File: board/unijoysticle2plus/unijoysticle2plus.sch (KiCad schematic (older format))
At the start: 44 parts, among them J1 DB9_Female, J2 DB9_Female, J3 USB_B_Micro, Q1 S8050, Q2 S8050, SW1 RESET, SW2 JOY SWAP, U1 74HC05, U2 74HC05, U3 74HC05, U4 ESP32-WROOM-32D, U5 AMS1117-3.3, U6 CH340C

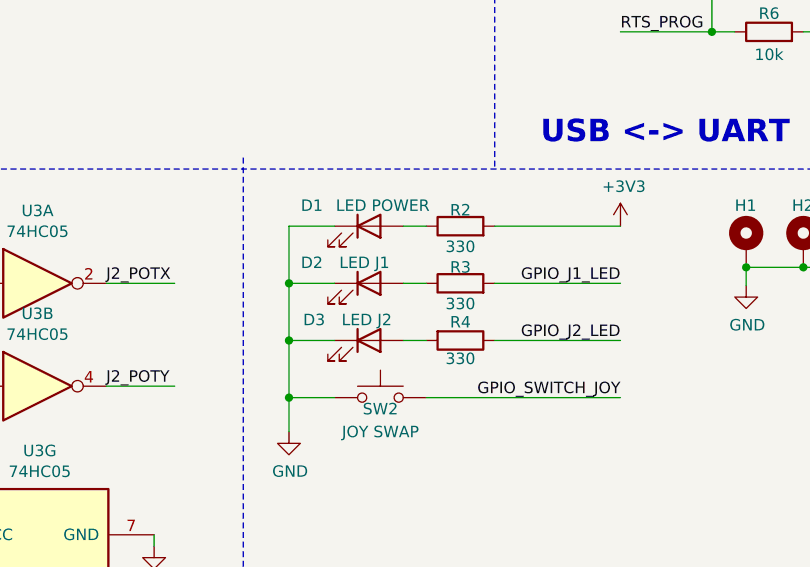
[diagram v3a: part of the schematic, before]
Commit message: unijoysticle2+: rev b. JLCPCB fixes
Add LCSC reference to new components
Update LCSC reference of old components to use 0805
Power plane in layer is split in 3: VCC (C64 5+), 3v3+ and VBUS
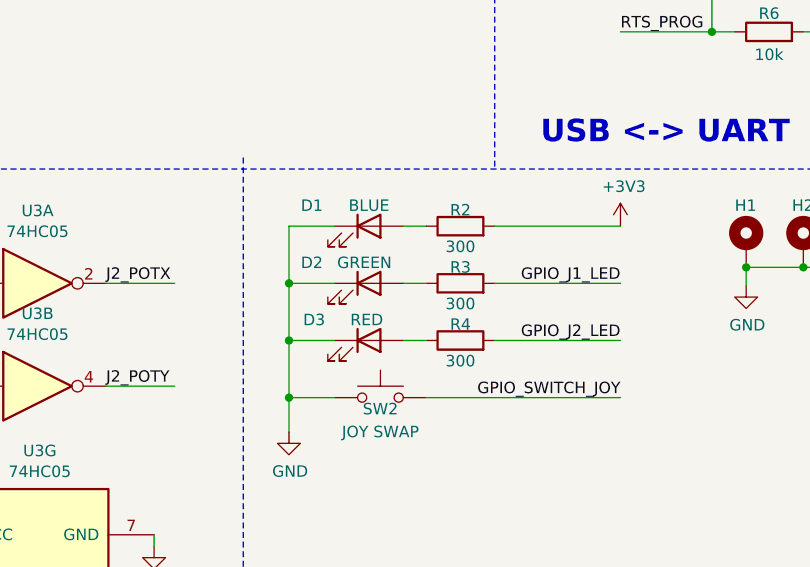
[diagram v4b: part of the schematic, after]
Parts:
- C1, C12, C2, C3, C4, C5: LCSC C1525 -> C49678
- C10: LCSC (none) -> C28323
- C11: LCSC (none) -> C49678
- C6, C8, C9: LCSC C59461 -> C45783
- D1: value LED POWER -> BLUE; LCSC (none) -> C389525
- D2: value LED J1 -> GREEN; LCSC (none) -> C188728
- D3: value LED J2 -> RED; LCSC (none) -> C84256
- R1, R5, R6: LCSC C25744 -> C17414
- R2, R3, R4: value 330 -> 300; LCSC (none) -> C17617
- R7, R8: LCSC (none) -> C17513
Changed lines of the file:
@@
 P 6150 6000
 F 0 "D2" H 5900 6090 50  0000 C CNN
-F 1 "LED J1" H 6130 6090 50  0000 C CNN
+F 1 "GREEN" H 6130 6090 50  0000 C CNN
 F 2 "LED_SMD:LED_0805_2012Metric_Pad1.15x1.40mm_HandSolder" H 6150 6000 50  0001 C CNN
 F 3 "~" H 6150 6000 50  0001 C CNN
-F 4 "" H 6150 6000 50  0001 C CNN "LCSC"
+F 4 "C188728" H 6150 6000 50  0001 C CNN "LCSC"
 	1    6150 6000
 	1    0    0    -1
@@
 P 6150 6250
 F 0 "D3" H 5910 6340 50  0000 C CNN
-F 1 "LED J2" H 6140 6340 50  0000 C CNN
+F 1 "RED" H 6140 6340 50  0000 C CNN
 F 2 "LED_SMD:LED_0805_2012Metric_Pad1.15x1.40mm_HandSolder" H 6150 6250 50  0001 C CNN
 F 3 "~" H 6150 6250 50  0001 C CNN
-F 4 "" H 6150 6250 50  0001 C CNN "LCSC"
+F 4 "C84256" H 6150 6250 50  0001 C CNN "LCSC"
 	1    6150 6250
 	1    0    0    -1
@@
 Wire Wire Line
 	6400 6500 7250 6500
-$Comp
-L Device:R R4
-U 1 1 5F9908EC
-P 6550 6250
-F 0 "R4" V 6470 6250 50  0000 C CNN
-F 1 "330" V 6630 6250 50  0000 C CNN
-F 2 "Resistor_SMD:R_0805_2012Metric_Pad1.20x1.40mm_HandSolder" V 6480 6250 50  0001 C CNN
-F 3 "~" H 6550 6250 50  0001 C CNN
-F 4 "" V 6550 6250 50  0001 C CNN "LCSC"
-	1    6550 6250
-	0    1    1    0
-$EndComp
 Wire Wire Line
 	6700 6000 7250 6000
@@
 F 2 "Capacitor_SMD:C_0805_2012Metric_Pad1.18x1.45mm_HandSolder" H 8300 1200 50  0001 C CNN
 F 3 "~" H 8300 1200 50  0001 C CNN
-F 4 "C59461" H 8300 1200 50  0001 C CNN "LCSC"
+F 4 "C45783" H 8300 1200 50  0001 C CNN "LCSC"
 	1    8300 1200
 	1    0    0    -1
@@
 F 2 "Capacitor_SMD:C_0805_2012Metric_Pad1.18x1.45mm_HandSolder" H 9200 1200 50  0001 C CNN
 F 3 "~" H 9200 1200 50  0001 C CNN
-F 4 "C59461" H 9200 1200 50  0001 C CNN "LCSC"
+F 4 "C45783" H 9200 1200 50  0001 C CNN "LCSC"
 	1    9200 1200
 	1    0    0    -1
@@
 F 2 "Resistor_SMD:R_0805_2012Metric_Pad1.20x1.40mm_HandSolder" V 7830 4350 50  0001 C CNN
 F 3 "~" H 7900 4350 50  0001 C CNN
-F 4 "C25744" V 7900 4350 50  0001 C CNN "LCSC"
+F 4 "C17414" V 7900 4350 50  0001 C CNN "LCSC"
 	1    7900 4350
 	0    1    1    0
@@
 F 2 "Resistor_SMD:R_0805_2012Metric_Pad1.20x1.40mm_HandSolder" V 7830 4900 50  0001 C CNN
 F 3 "~" H 7900 4900 50  0001 C CNN
-F 4 "C25744" V 7900 4900 50  0001 C CNN "LCSC"
+F 4 "C17414" V 7900 4900 50  0001 C CNN "LCSC"
 	1    7900 4900
 	0    -1   -1   0
@@
 F 2 "Capacitor_SMD:C_0805_2012Metric_Pad1.18x1.45mm_HandSolder" H 6000 1050 50  0001 C CNN
 F 3 "~" H 6000 1050 50  0001 C CNN
-F 4 "C59461" H 6000 1050 50  0001 C CNN "LCSC"
+F 4 "C45783" H 6000 1050 50  0001 C CNN "LCSC"
 	1    6000 1050
 	-1   0    0    1
@@
 F 2 "Capacitor_SMD:C_0805_2012Metric_Pad1.18x1.45mm_HandSolder" H 5600 1050 50  0001 C CNN
 F 3 "~" H 5600 1050 50  0001 C CNN
-F 4 "C1525" H 5600 1050 50  0001 C CNN "LCSC"
+F 4 "C49678" H 5600 1050 50  0001 C CNN "LCSC"
 	1    5600 1050
 	1    0    0    -1
@@
 F 2 "Capacitor_SMD:C_0805_2012Metric_Pad1.18x1.45mm_HandSolder" H 4210 7200 50  0001 C CNN
 F 3 "~" H 4210 7200 50  0001 C CNN
-F 4 "C1525" H 4210 7200 50  0001 C CNN "LCSC"
+F 4 "C49678" H 4210 7200 50  0001 C CNN "LCSC"
 	1    4210 7200
 	1    0    0    -1
@@
 F 2 "Capacitor_SMD:C_0805_2012Metric_Pad1.18x1.45mm_HandSolder" H 2560 7150 50  0001 C CNN
 F 3 "~" H 2560 7150 50  0001 C CNN
-F 4 "C1525" H 2560 7150 50  0001 C CNN "LCSC"
+F 4 "C49678" H 2560 7150 50  0001 C CNN "LCSC"
 	1    2560 7150
 	1    0    0    -1
@@
 F 2 "Capacitor_SMD:C_0805_2012Metric_Pad1.18x1.45mm_HandSolder" H 760 7150 50  0001 C CNN
 F 3 "~" H 760 7150 50  0001 C CNN
-F 4 "C1525" H 760 7150 50  0001 C CNN "LCSC"
+F 4 "C49678" H 760 7150 50  0001 C CNN "LCSC"
 	1    760  7150
 	1    0    0    -1
@@
 P 6150 5750
 F 0 "D1" H 5900 5840 50  0000 C CNN
-F 1 "LED POWER" H 6210 5840 50  0000 C CNN
+F 1 "BLUE" H 6150 5840 50  0000 C CNN
 F 2 "LED_SMD:LED_0805_2012Metric_Pad1.15x1.40mm_HandSolder" H 6150 5750 50  0001 C CNN
 F 3 "~" H 6150 5750 50  0001 C CNN
-F 4 "" H 6150 5750 50  0001 C CNN "LCSC"
+F 4 "C389525" H 6150 5750 50  0001 C CNN "LCSC"
 	1    6150 5750
 	1    0    0    -1
@@
 P 6550 5750
 F 0 "R2" V 6620 5750 50  0000 C CNN
-F 1 "330" V 6460 5750 50  0000 C CNN
+F 1 "300" V 6460 5750 50  0000 C CNN
 F 2 "Resistor_SMD:R_0805_2012Metric_Pad1.20x1.40mm_HandSolder" V 6480 5750 50  0001 C CNN
 F 3 "~" H 6550 5750 50  0001 C CNN
-F 4 "" V 6550 5750 50  0001 C CNN "LCSC"
+F 4 "C17617" V 6550 5750 50  0001 C CNN "LCSC"
 	1    6550 5750
 	0    -1   -1   0
@@
 P 6550 6000
 F 0 "R3" V 6620 6000 50  0000 C CNN
-F 1 "330" V 6460 6000 50  0000 C CNN
+F 1 "300" V 6460 6000 50  0000 C CNN
 F 2 "Resistor_SMD:R_0805_2012Metric_Pad1.20x1.40mm_HandSolder" V 6480 6000 50  0001 C CNN
 F 3 "~" H 6550 6000 50  0001 C CNN
-F 4 "" V 6550 6000 50  0001 C CNN "LCSC"
+F 4 "C17617" V 6550 6000 50  0001 C CNN "LCSC"
 	1    6550 6000
 	0    -1   -1   0
@@
 F 2 "Capacitor_SMD:C_0805_2012Metric_Pad1.18x1.45mm_HandSolder" H 3550 2480 50  0001 C CNN
 F 3 "~" H 3550 2480 50  0001 C CNN
-F 4 "C1525" V 3550 2480 50  0001 C CNN "LCSC"
+F 4 "C49678" V 3550 2480 50  0001 C CNN "LCSC"
 	1    3550 2480
 	0    -1   -1   0
@@
 F 2 "Resistor_SMD:R_0805_2012Metric_Pad1.20x1.40mm_HandSolder" V 4030 1270 50  0001 C CNN
 F 3 "~" H 4100 1270 50  0001 C CNN
-F 4 "C25744" V 4100 1270 50  0001 C CNN "LCSC"
+F 4 "C17414" V 4100 1270 50  0001 C CNN "LCSC"
 	1    4100 1270
 	-1   0    0    1
@@
 F 2 "Capacitor_SMD:C_0805_2012Metric_Pad1.18x1.45mm_HandSolder" H 4100 1700 50  0001 C CNN
 F 3 "~" H 4100 1700 50  0001 C CNN
-F 4 "C1525" H 4100 1700 50  0001 C CNN "LCSC"
+F 4 "C49678" H 4100 1700 50  0001 C CNN "LCSC"
 	1    4100 1700
 	1    0    0    -1
@@
 F 2 "Capacitor_SMD:C_0805_2012Metric_Pad1.18x1.45mm_HandSolder" H 9150 3050 50  0001 C CNN
 F 3 "~" H 9150 3050 50  0001 C CNN
+F 4 "C28323" H 9150 3050 50  0001 C CNN "LCSC"
 	1    9150 3050
 	1    0    0    -1
@@
 F 2 "Capacitor_SMD:C_0805_2012Metric_Pad1.18x1.45mm_HandSolder" H 10480 1920 50  0001 C CNN
 F 3 "~" H 10480 1920 50  0001 C CNN
+F 4 "C49678" H 10480 1920 50  0001 C CNN "LCSC"
 	1    10480 1920
 	1    0    0    -1
@@
 F 2 "Resistor_SMD:R_0805_2012Metric_Pad1.20x1.40mm_HandSolder" H 10180 2340 50  0001 C CNN
 F 3 "~" H 10180 2340 50  0001 C CNN
+F 4 "C17513" V 10180 2340 50  0001 C CNN "LCSC"
 	1    10180 2340
 	0    1    1    0
@@
 F 2 "Resistor_SMD:R_0805_2012Metric_Pad1.20x1.40mm_HandSolder" H 10180 2440 50  0001 C CNN
 F 3 "~" H 10180 2440 50  0001 C CNN
+F 4 "C17513" V 10180 2440 50  0001 C CNN "LCSC"
 	1    10180 2440
 	0    1    1    0
@@
 Wire Wire Line
 	10280 2440 10620 2440
+$Comp
+L Device:R R4
+U 1 1 61258BA1
+P 6550 6250
+F 0 "R4" V 6620 6250 50  0000 C CNN
+F 1 "300" V 6460 6250 50  0000 C CNN
+F 2 "Resistor_SMD:R_0805_2012Metric_Pad1.20x1.40mm_HandSolder" V 6480 6250 50  0001 C CNN
+F 3 "~" H 6550 6250 50  0001 C CNN
+F 4 "C17617" V 6550 6250 50  0001 C CNN "LCSC"
+	1    6550 6250
+	0    -1   -1   0
+$EndComp
 $EndSCHEMATC

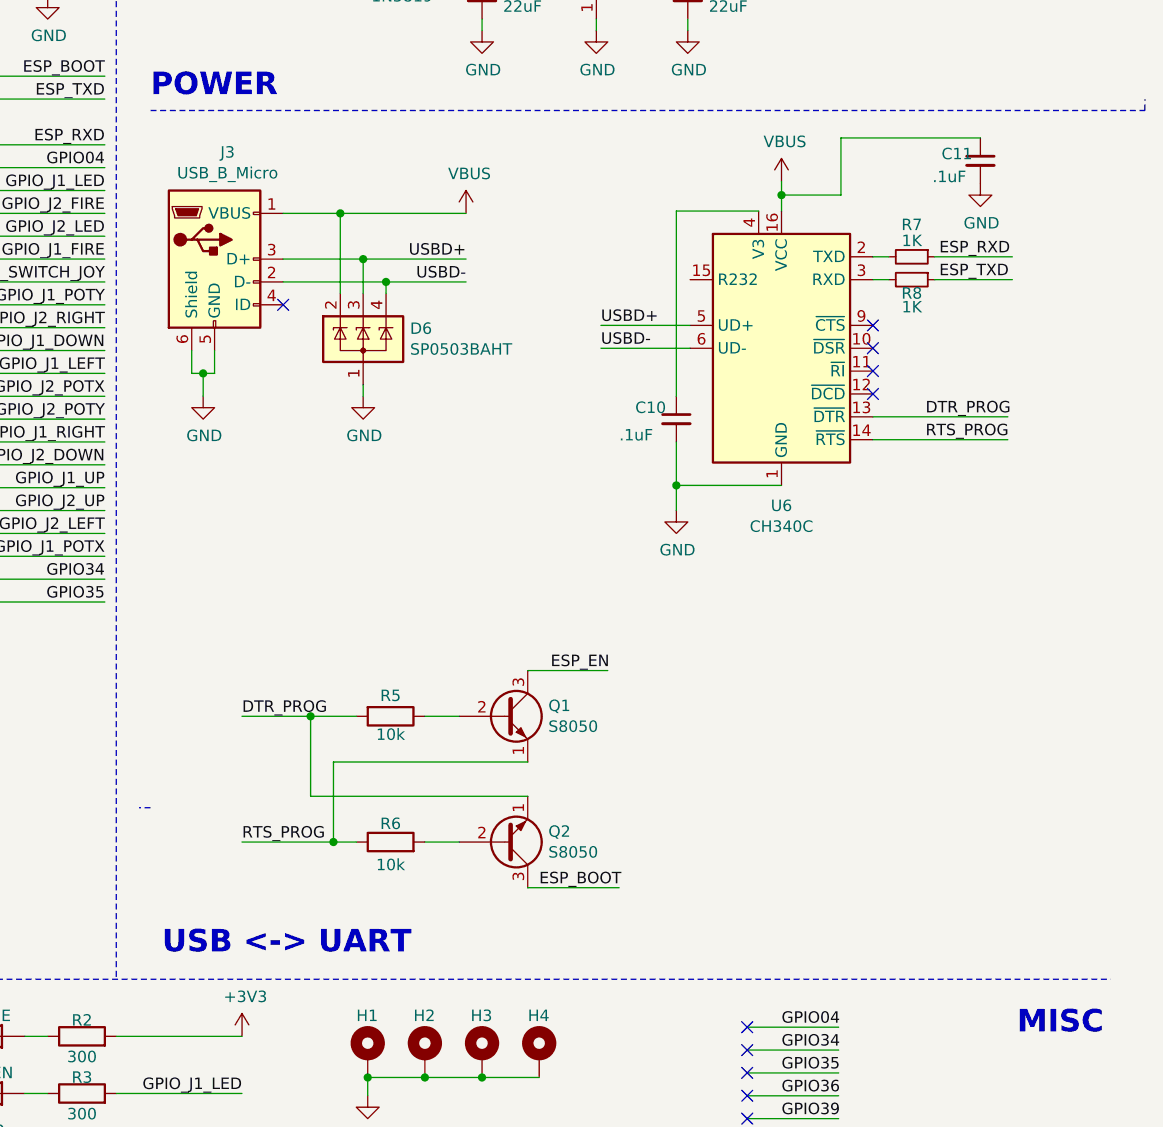
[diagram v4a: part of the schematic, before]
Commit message: Unijoysticle2+: Rev C. WIP
Although I haven't tested yet Rev B., there a few changes that I wanted
to make to it.
Rev. C, so far, has the following changes:

- Switch Power plane with Ground place: Ground plane is #2 and Power
  plane #3.
- Manually routed: No longer uses auto-route. I think it is better for
  debugging to route it manually. More vias. Vias placed closer to the
  pads. Might reduce inductance (?).
- No longer using the ESD protector for USB. Almost nobody uses it,
  besides that CP2104 recommends it. But I'm no longer using CP2104, and
  CH340 doesn't mention it... I think it would be a good idea
  nonetheless, but only as an optional feature.
- Differential pair routing for USB D- and USB D+
- Mounting holes moved a tiny bit closer to the corners

Again, Rev. B might work perfectly well... waiting for it to arrive. But
I just wanted to make the above mentioned changes.
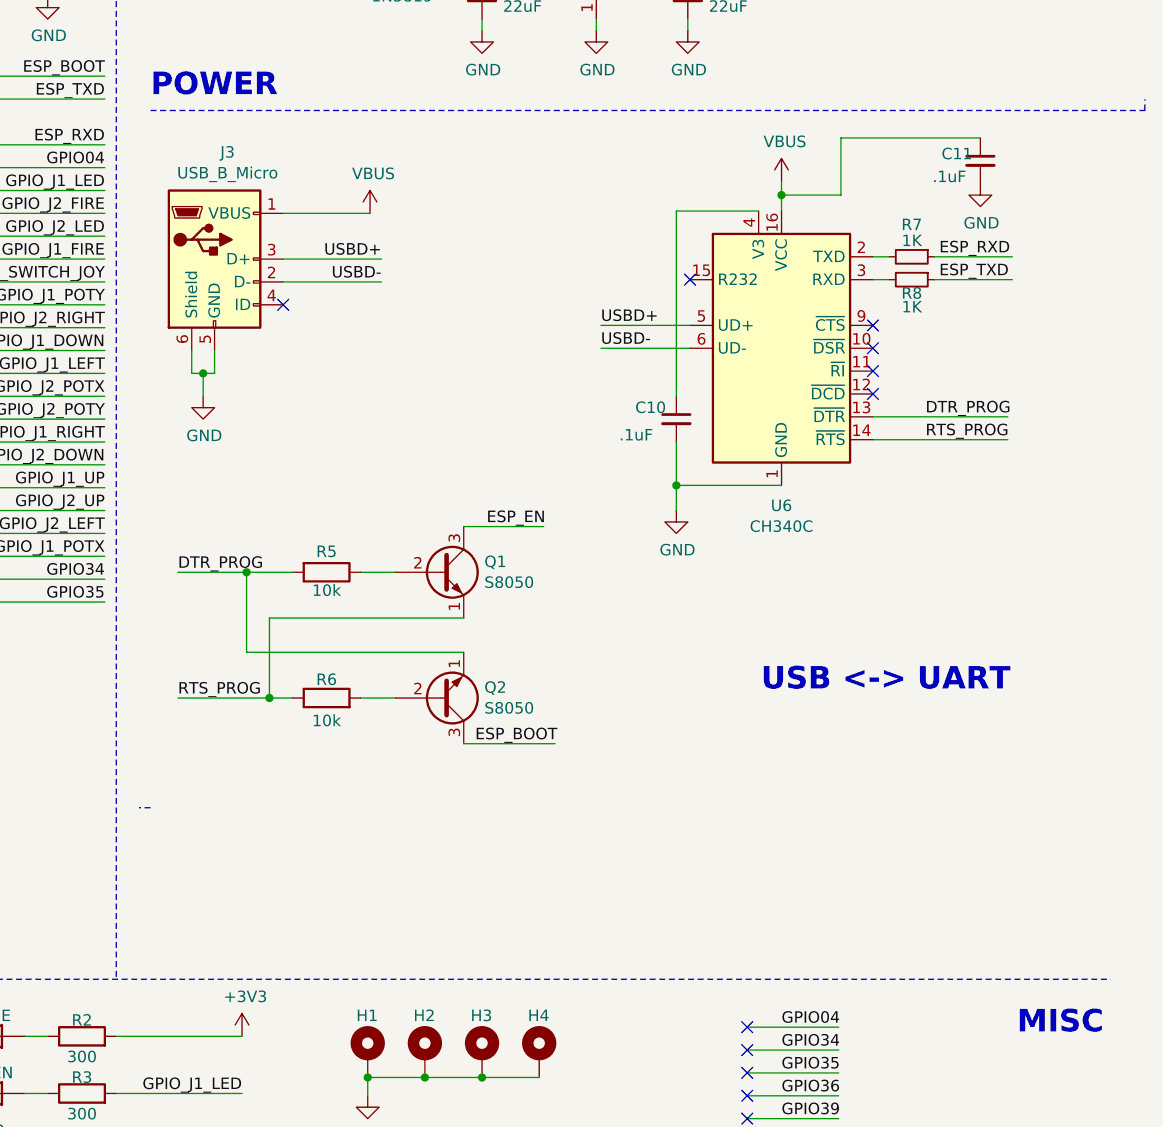
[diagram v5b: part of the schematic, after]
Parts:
- removed D6: SP0503BAHT, Package_TO_SOT_SMD:SOT-143, symbol Power_Protection:SP0503BAHT
- R9: footprint Resistor_SMD:R_1206_3216Metric_Pad1.30x1.75mm_HandSolder -> Resistor_SMD:R_0805_2012Metric_Pad1.20x1.40mm_HandSolder; LCSC C17888 -> C17477
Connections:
- wire segments 196 -> 189
- no-connect marks 17 -> 18
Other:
- moved on the sheet: Q1, Q2, R5, R6
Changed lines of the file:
@@
 Sheet 1 1
 Title "Unijoysticle 2+"
-Date "2021-06-22"
-Rev "B"
+Date "2021-06-25"
+Rev "C"
 Comp "Retro Moe"
 Comment1 ""
@@
 	1    0    0    -1
 $EndComp
-Wire Wire Line
-	7680 2500 7680 2150
-Wire Wire Line
-	7680 2150 7430 2150
-$Comp
-L power:GND #PWR023
-U 1 1 5FCD484D
-P 7780 2950
-F 0 "#PWR023" H 7780 2700 50  0001 C CNN
-F 1 "GND" H 7785 2777 50  0000 C CNN
-F 2 "" H 7780 2950 50  0001 C CNN
-F 3 "" H 7780 2950 50  0001 C CNN
-	1    7780 2950
-	1    0    0    -1
-$EndComp
-Text Label 8230 2350 2    50   ~ 0
+Text Label 7860 2350 2    50   ~ 0
 USBD+
-Text Label 8230 2450 2    50   ~ 0
+Text Label 7860 2450 2    50   ~ 0
 USBD-
-Connection ~ 7680 2150
 $Comp
 L Diode:1N5819 D4
@@
 	-1   0    0    1
 $EndComp
-Wire Wire Line
-	7680 2150 8230 2150
 $Comp
 L power:VBUS #PWR025
 U 1 1 5FD77036
-P 8230 2150
-F 0 "#PWR025" H 8230 2000 50  0001 C CNN
-F 1 "VBUS" H 8245 2323 50  0000 C CNN
-F 2 "" H 8230 2150 50  0001 C CNN
-F 3 "" H 8230 2150 50  0001 C CNN
-	1    8230 2150
+P 7810 2150
+F 0 "#PWR025" H 7810 2000 50  0001 C CNN
+F 1 "VBUS" H 7825 2323 50  0000 C CNN
+F 2 "" H 7810 2150 50  0001 C CNN
+F 3 "" H 7810 2150 50  0001 C CNN
+	1    7810 2150
 	1    0    0    -1
 $EndComp
@@
 $EndComp
 Wire Wire Line
-	8500 5100 8900 5100
-Wire Wire Line
-	8200 4350 8050 4350
-Wire Wire Line
-	8200 4900 8050 4900
+	8220 4470 8620 4470
+Wire Wire Line
+	7920 3720 7770 3720
+Wire Wire Line
+	7920 4270 7770 4270
 $Comp
 L Device:R R5
 U 1 1 60AF2CFC
-P 7900 4350
-F 0 "R5" V 7810 4350 50  0000 C CNN
-F 1 "10k" V 7980 4350 50  0000 C CNN
-F 2 "Resistor_SMD:R_0805_2012Metric_Pad1.20x1.40mm_HandSolder" V 7830 4350 50  0001 C CNN
-F 3 "~" H 7900 4350 50  0001 C CNN
-F 4 "C17414" V 7900 4350 50  0001 C CNN "LCSC"
-	1    7900 4350
+P 7620 3720
+F 0 "R5" V 7530 3720 50  0000 C CNN
+F 1 "10k" V 7700 3720 50  0000 C CNN
+F 2 "Resistor_SMD:R_0805_2012Metric_Pad1.20x1.40mm_HandSolder" V 7550 3720 50  0001 C CNN
+F 3 "~" H 7620 3720 50  0001 C CNN
+F 4 "C17414" V 7620 3720 50  0001 C CNN "LCSC"
+	1    7620 3720
 	0    1    1    0
 $EndComp
@@
 L Device:R R6
 U 1 1 60AF3FED
-P 7900 4900
-F 0 "R6" V 7980 4900 50  0000 C CNN
-F 1 "10k" V 7800 4900 50  0000 C CNN
-F 2 "Resistor_SMD:R_0805_2012Metric_Pad1.20x1.40mm_HandSolder" V 7830 4900 50  0001 C CNN
-F 3 "~" H 7900 4900 50  0001 C CNN
-F 4 "C17414" V 7900 4900 50  0001 C CNN "LCSC"
-	1    7900 4900
+P 7620 4270
+F 0 "R6" V 7700 4270 50  0000 C CNN
+F 1 "10k" V 7520 4270 50  0000 C CNN
+F 2 "Resistor_SMD:R_0805_2012Metric_Pad1.20x1.40mm_HandSolder" V 7550 4270 50  0001 C CNN
+F 3 "~" H 7620 4270 50  0001 C CNN
+F 4 "C17414" V 7620 4270 50  0001 C CNN "LCSC"
+	1    7620 4270
 	0    -1   -1   0
 $EndComp
 Wire Wire Line
-	7750 4350 7550 4350
-Wire Wire Line
-	7750 4900 7650 4900
-Wire Wire Line
-	8500 4550 7650 4550
-Wire Wire Line
-	7650 4550 7650 4900
-Connection ~ 7650 4900
-Wire Wire Line
-	7550 4350 7550 4700
-Wire Wire Line
-	7550 4350 7250 4350
-Connection ~ 7550 4350
-Wire Wire Line
-	7250 4900 7650 4900
-Wire Wire Line
-	8500 4150 8850 4150
+	7470 3720 7270 3720
+Wire Wire Line
+	7470 4270 7370 4270
+Wire Wire Line
+	8220 3920 7370 3920
+Wire Wire Line
+	7370 3920 7370 4270
+Connection ~ 7370 4270
+Wire Wire Line
+	7270 3720 7270 4070
+Wire Wire Line
+	7270 3720 6970 3720
+Connection ~ 7270 3720
+Wire Wire Line
+	6970 4270 7370 4270
+Wire Wire Line
+	8220 3520 8570 3520
 $Comp
 L Connector:USB_B_Micro J3
@@
 	1    0    0    -1
 $EndComp
-Text Label 7250 4350 0    50   ~ 0
+Text Label 6970 3720 0    50   ~ 0
 DTR_PROG
-Text Label 7250 4900 0    50   ~ 0
+Text Label 6970 4270 0    50   ~ 0
 RTS_PROG
-Text Label 8550 5100 0    50   ~ 0
+Text Label 8270 4470 0    50   ~ 0
 ESP_BOOT
-Text Label 8600 4150 0    50   ~ 0
+Text Label 8320 3520 0    50   ~ 0
 ESP_EN
 Wire Wire Line
@@
 L Transistor_BJT:S8050 Q1
 U 1 1 60C0C352
-P 8400 4350
-F 0 "Q1" H 8590 4396 50  0000 L CNN
-F 1 "S8050" H 8590 4305 50  0000 L CNN
-F 2 "Package_TO_SOT_SMD:SOT-23" H 8600 4275 50  0001 L CIN
-F 3 "http://www.unisonic.com.tw/datasheet/S8050.pdf" H 8400 4350 50  0001 L CNN
-F 4 "C2150" H 8400 4350 50  0001 C CNN "LCSC"
-	1    8400 4350
+P 8120 3720
+F 0 "Q1" H 8310 3766 50  0000 L CNN
+F 1 "S8050" H 8310 3675 50  0000 L CNN
+F 2 "Package_TO_SOT_SMD:SOT-23" H 8320 3645 50  0001 L CIN
+F 3 "http://www.unisonic.com.tw/datasheet/S8050.pdf" H 8120 3720 50  0001 L CNN
+F 4 "C2150" H 8120 3720 50  0001 C CNN "LCSC"
+	1    8120 3720
 	1    0    0    -1
 $EndComp
@@
 L Transistor_BJT:S8050 Q2
 U 1 1 60C0CCE3
-P 8400 4900
-F 0 "Q2" H 8590 4854 50  0000 L CNN
-F 1 "S8050" H 8590 4945 50  0000 L CNN
-F 2 "Package_TO_SOT_SMD:SOT-23" H 8600 4825 50  0001 L CIN
-F 3 "http://www.unisonic.com.tw/datasheet/S8050.pdf" H 8400 4900 50  0001 L CNN
-F 4 "C2150" H 8400 4900 50  0001 C CNN "LCSC"
-	1    8400 4900
+P 8120 4270
+F 0 "Q2" H 8310 4224 50  0000 L CNN
+F 1 "S8050" H 8310 4315 50  0000 L CNN
+F 2 "Package_TO_SOT_SMD:SOT-23" H 8320 4195 50  0001 L CIN
+F 3 "http://www.unisonic.com.tw/datasheet/S8050.pdf" H 8120 4270 50  0001 L CNN
+F 4 "C2150" H 8120 4270 50  0001 C CNN "LCSC"
+	1    8120 4270
 	1    0    0    1
 $EndComp
 Wire Wire Line
-	7550 4700 8500 4700
+	7270 4070 8220 4070
 $Comp
 L power:+3V3 #PWR013
@@
 	1    0    0    -1
 $EndComp
-$Comp
-L Power_Protection:SP0503BAHT D6
-U 1 1 60C4C799
-P 7780 2700
-F 0 "D6" H 7985 2746 50  0000 L CNN
-F 1 "SP0503BAHT" H 7985 2655 50  0000 L CNN
-F 2 "Package_TO_SOT_SMD:SOT-143" H 8005 2650 50  0001 L CNN
-F 3 "http://www.littelfuse.com/~/media/files/littelfuse/technical%20resources/documents/data%20sheets/sp05xxba.pdf" H 7905 2825 50  0001 C CNN
-F 4 "C720028" H 7780 2700 50  0001 C CNN "LCSC"
-	1    7780 2700
-	1    0    0    -1
-$EndComp
-Wire Wire Line
-	7780 2900 7780 2950
-Wire Wire Line
-	7430 2350 7780 2350
-Wire Wire Line
-	7430 2450 7880 2450
-Wire Wire Line
-	7780 2500 7780 2350
-Connection ~ 7780 2350
-Wire Wire Line
-	7780 2350 8230 2350
-Wire Wire Line
-	7880 2500 7880 2450
-Connection ~ 7880 2450
-Wire Wire Line
-	7880 2450 8230 2450
 Wire Notes Line
 	6850 1700 11200 1700
@@
 Text Notes 6850 1650 0    98   ~ 20
 POWER
-Text Notes 6900 5400 0    98   ~ 20
+Text Notes 9520 4250 0    98   ~ 20
 USB <-> UART
 Text Notes 3150 700  0    98   ~ 20
@@
 F 0 "R9" V 3920 2310 50  0000 C CNN
 F 1 "0" V 4090 2310 50  0000 C CNN
-F 2 "Resistor_SMD:R_1206_3216Metric_Pad1.30x1.75mm_HandSolder" V 3940 2310 50  0001 C CNN
+F 2 "Resistor_SMD:R_0805_2012Metric_Pad1.20x1.40mm_HandSolder" V 3940 2310 50  0001 C CNN
 F 3 "~" H 4010 2310 50  0001 C CNN
-F 4 "C17888" V 4010 2310 50  0001 C CNN "LCSC"
+F 4 "C17477" V 4010 2310 50  0001 C CNN "LCSC"
 	1    4010 2310
 	0    1    1    0
@@
 	0    -1   -1   0
 $EndComp
+Wire Wire Line
+	7430 2450 7860 2450
+Wire Wire Line
+	7430 2350 7860 2350
+Wire Wire Line
+	7430 2150 7810 2150
+NoConn ~ 9210 2440
 $EndSCHEMATC
